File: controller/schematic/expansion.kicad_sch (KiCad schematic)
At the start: 24 parts, among them J10 DRY_IN, J8 EXPANSION, J9 I2C_SENSOR, U18 TPD4E05U06DQA, U6 TPD4E05U06DQA, U7 TPD4E05U06DQA

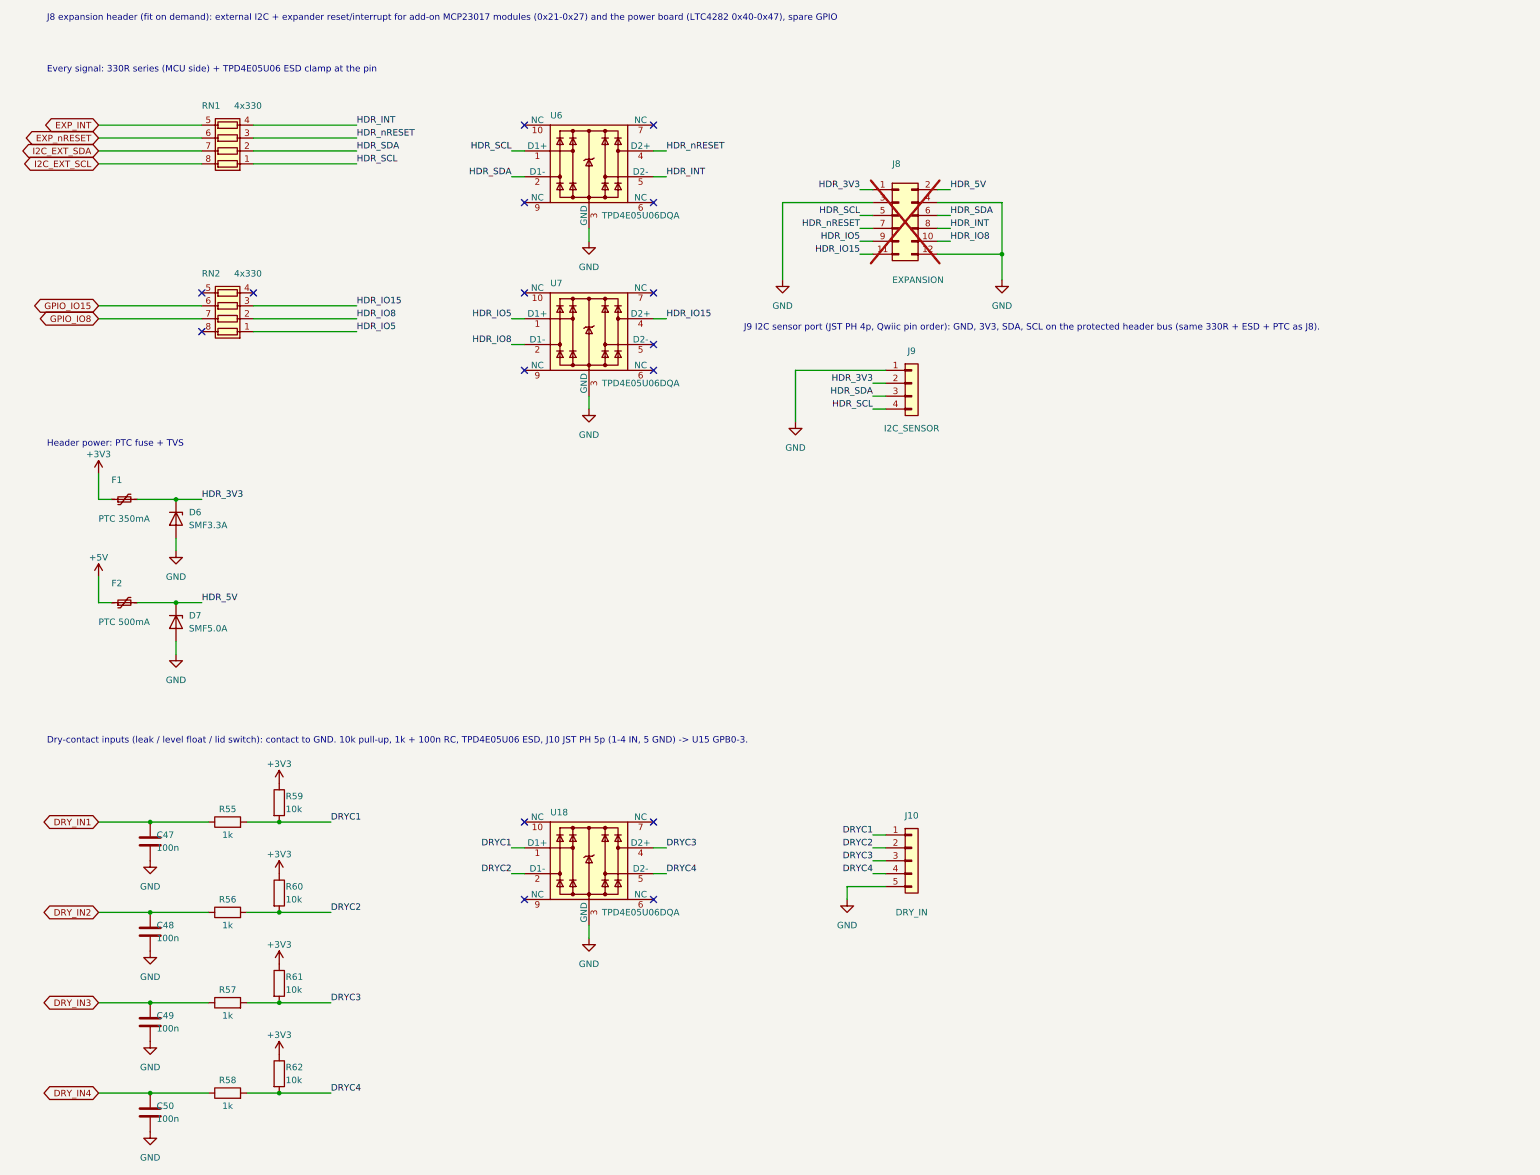
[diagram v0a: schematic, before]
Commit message: controller: rev D schematic - node section (relays sheet: J11-J18, K1-K16, U14-U17 and passives), J8 expansion header network (RN2, U7, F2, D7, R19, EXP_nRESET) and the 19 V input (J3, F3, D1, D8) removed; two 12 V PH 2p inputs J11 / J12 OR-ed by SS34 D10 / D11 with SMAJ15A D12 (C148216), VIN_SENSE divider 68k / 10k; new Plane link sheet: J13 / J14 PH 5p, 2.2k SDA / SCL and 10k EXP_INT pull-ups, 33R series, TPD4E05U06 U19 / U20, TPS2553DBVR load switches U21 / U22 (C55266, R_ILIM 180k, 129-174 mA) with a granite:TPS2553DBV symbol; MCU: plane link on GPIO2/3, TMP1075 and J9 on the local bus GPIO6/7, dry inputs on GPIO10/11/4/15, rev C GPIO4 pull-down gone; title blocks rev D; ERC 0, netlist pin map checked
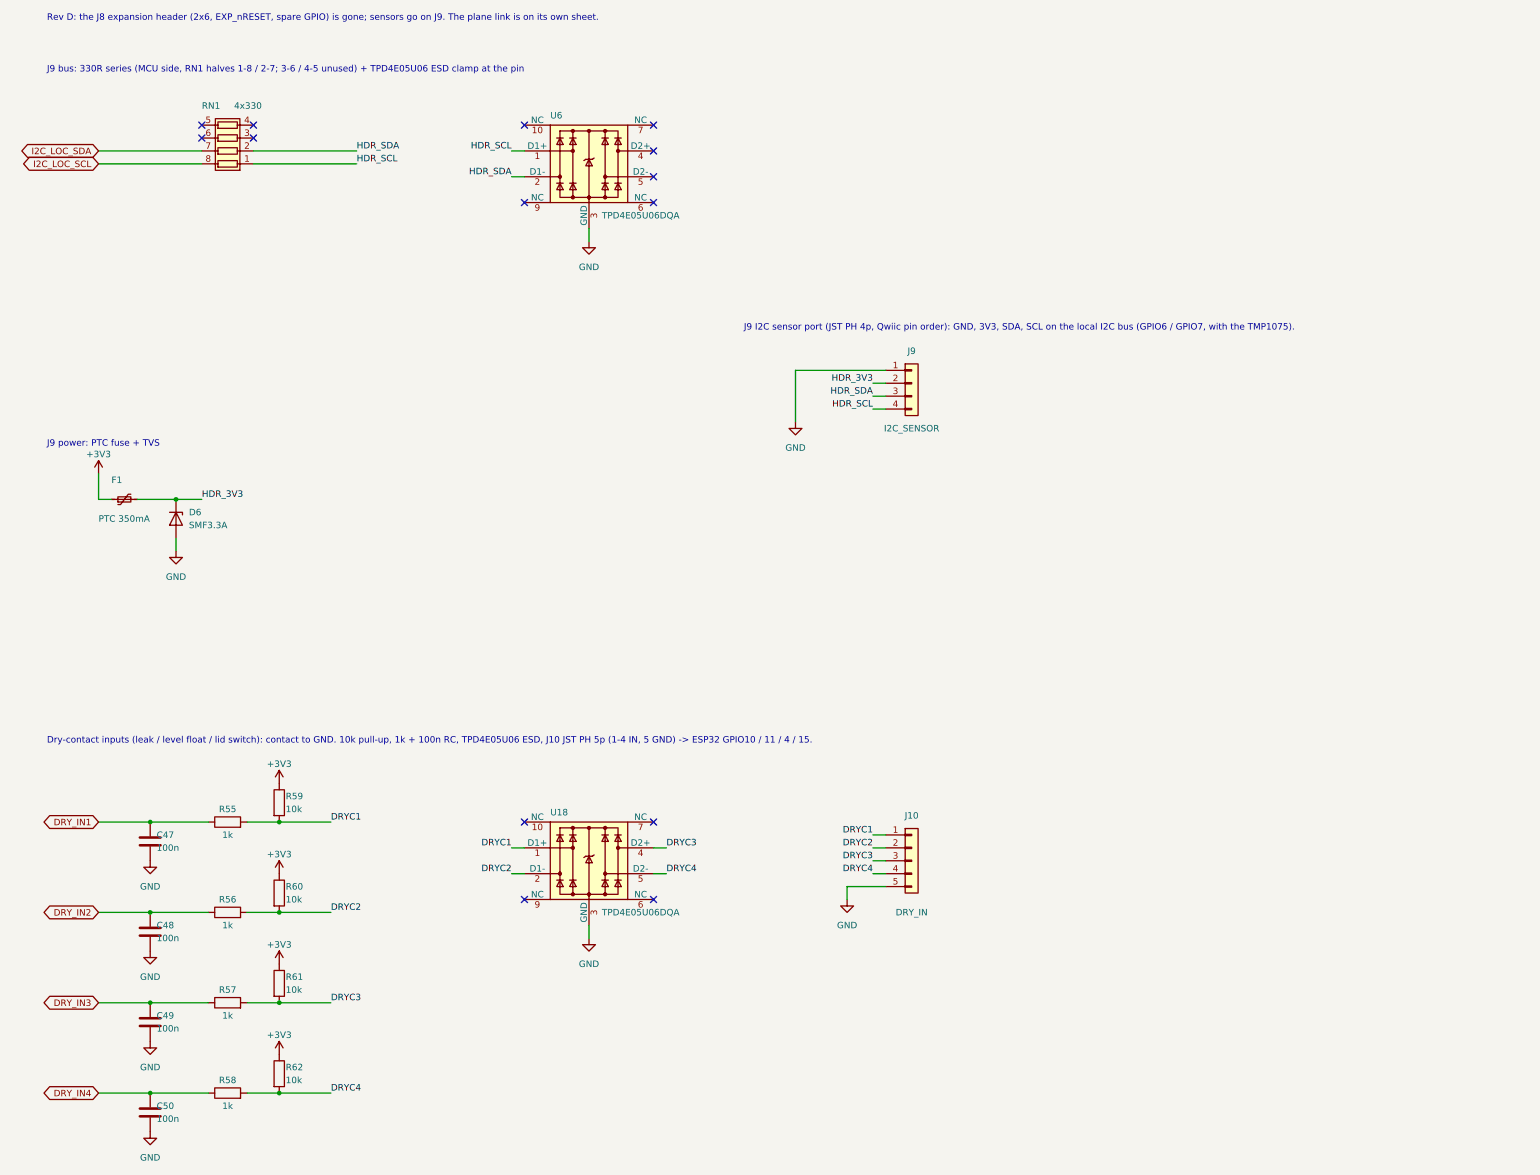
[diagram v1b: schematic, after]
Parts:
- removed D7: SMF5.0A, Diode_SMD:D_SOD-123F, symbol Device:D_Zener
- removed F2: PTC 500mA, Fuse:Fuse_1206_3216Metric, symbol Device:Polyfuse_Small
- removed J8: EXPANSION, Connector_PinHeader_2.54mm:PinHeader_2x06_P2.54mm_Vertical, symbol Connector_Generic:Conn_02x06_Odd_Even
- removed RN2: 4x330, Resistor_SMD:R_Array_Convex_4x0402, symbol Device:R_Pack04
- removed U7: TPD4E05U06DQA, Package_SON:USON-10_2.5x1.0mm_P0.5mm, symbol Power_Protection:TPD4E05U06DQA
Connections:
- net EXP_INT: no longer names the net of RN1.5 (R4.2)
- net EXP_nRESET: no longer names the net of RN1.6 (R3.2)
- net HDR_INT: no longer names the net of U6.5 (D2-)
- net HDR_INT: no longer RN1.4 (R4.1)
- net HDR_nRESET: no longer names the net of U6.4 (D2+)
- net HDR_nRESET: no longer RN1.3 (R3.1)
- net I2C_EXT_SCL renamed I2C_LOC_SCL
- net I2C_EXT_SDA renamed I2C_LOC_SDA
- no-connect marks 16 -> 14
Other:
- note added: "Dry-contact inputs (leak / level float / lid switch): contact to GND. 10k pull-up, 1k + 100n RC, TPD4E05U06 ESD, J10 JST PH 5p (1-4 IN, 5 GND) -> ESP32 GPIO10 / 11 / 4 / 15."
- note added: "J9 I2C sensor port (JST PH 4p, Qwiic pin order): GND, 3V3, SDA, SCL on the local I2C bus (GPIO6 / GPIO7, with the TMP1075)."
- note added: "J9 bus: 330R series (MCU side, RN1 halves 1-8 / 2-7; 3-6 / 4-5 unused) + TPD4E05U06 ESD clamp at the pin"
- note added: "J9 power: PTC fuse + TVS"
- note added: "Rev D: the J8 expansion header (2x6, EXP_nRESET, spare GPIO) is gone; sensors go on J9. The plane link is on its own sheet."
- note removed: "Dry-contact inputs (leak / level float / lid switch): contact to GND. 10k pull-up, 1k + 100n RC, TPD4E05U06 ESD, J10 JST PH 5p (1-4 IN, 5 GND) -> U15 GPB0-3."
- note removed: "Every signal: 330R series (MCU side) + TPD4E05U06 ESD clamp at the pin"
- note removed: "Header power: PTC fuse + TVS"
- note removed: "J8 expansion header (fit on demand): external I2C + expander reset/interrupt for add-on MCP23017 modules (0x21-0x27) and the power board (LTC4282 0x40-0x47), spare GPIO"
- note removed: "J9 I2C sensor port (JST PH 4p, Qwiic pin order): GND, 3V3, SDA, SCL on the protected header bus (same 330R + ESD + PTC as J8)."
- title: Granite Controller - Expansion header -> Granite controller rev D - Sensors and dry contacts
